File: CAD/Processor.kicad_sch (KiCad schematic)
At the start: 78 parts, among them M1 FID, M11 MOUNTING, M12 Logo_KICAD, M15 MOUNTING, M2 FID, M3 MOUNTING, M9 MOUNTING, U11 ATSAME70Q20B-AN, X1 ECS-120-10-33B-CKM-TR

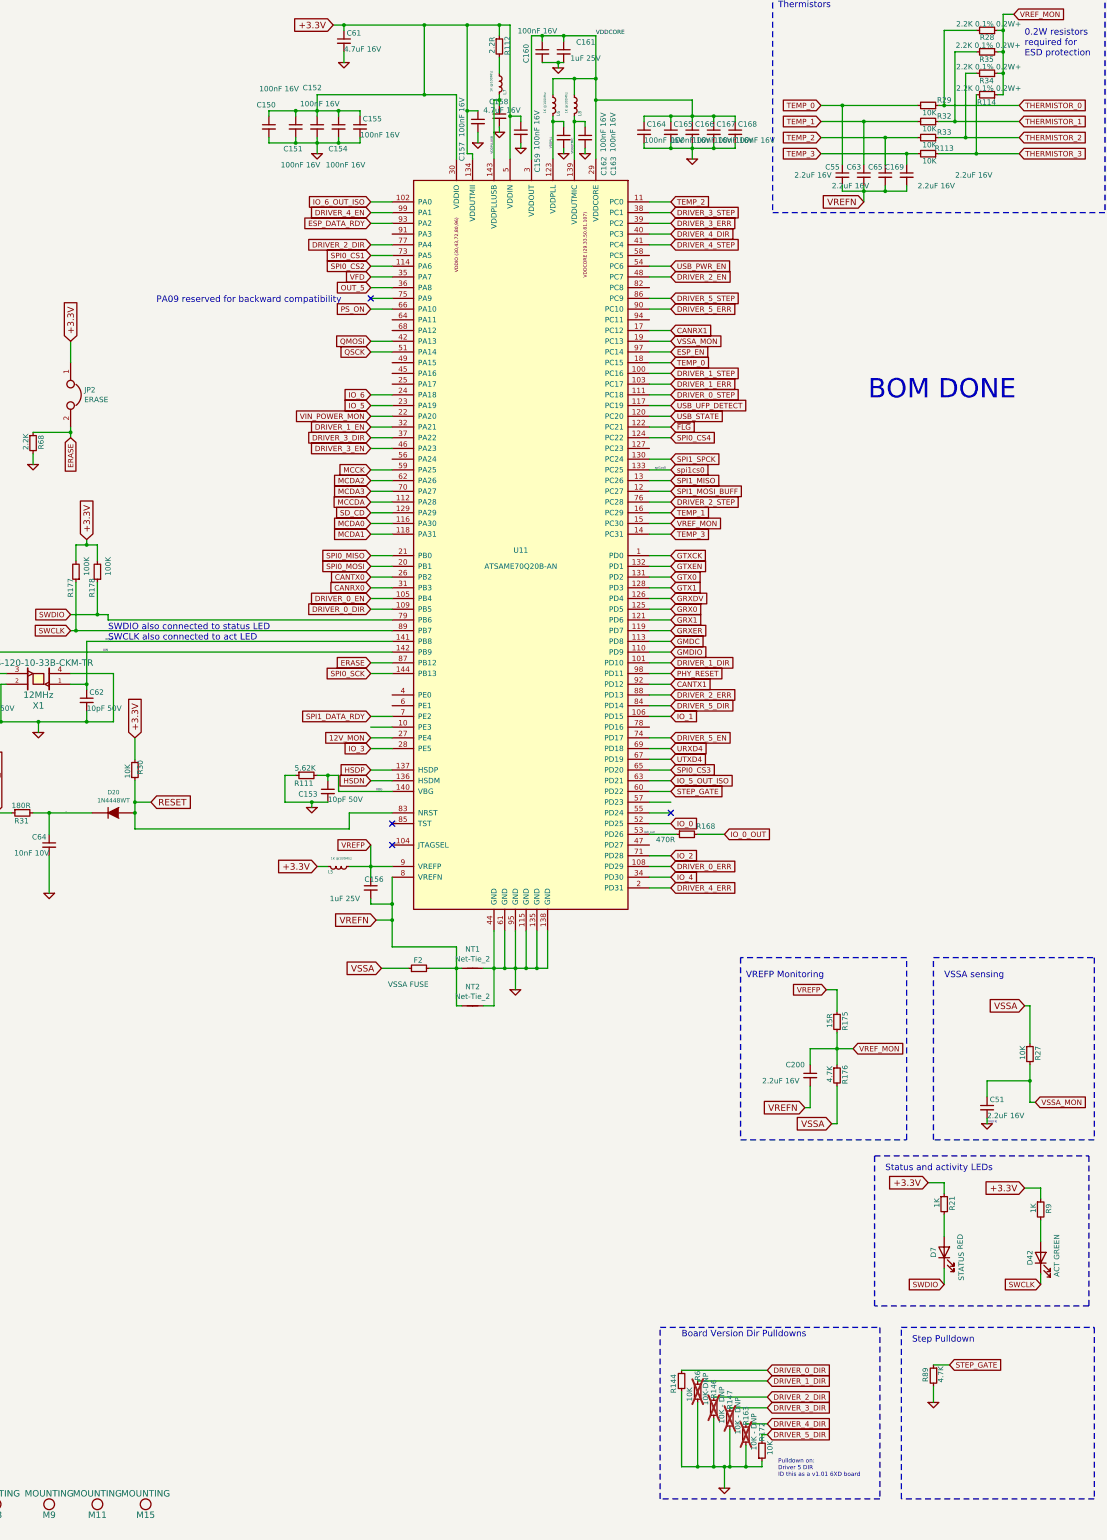
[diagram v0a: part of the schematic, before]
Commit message: WIP redoing board for new print
Removed version resistors.
Added pull-up on CMD.
Working on motors, not routed.
Added local library for custom parts.
Ran auto-cleanup of traces and vias (supervised).
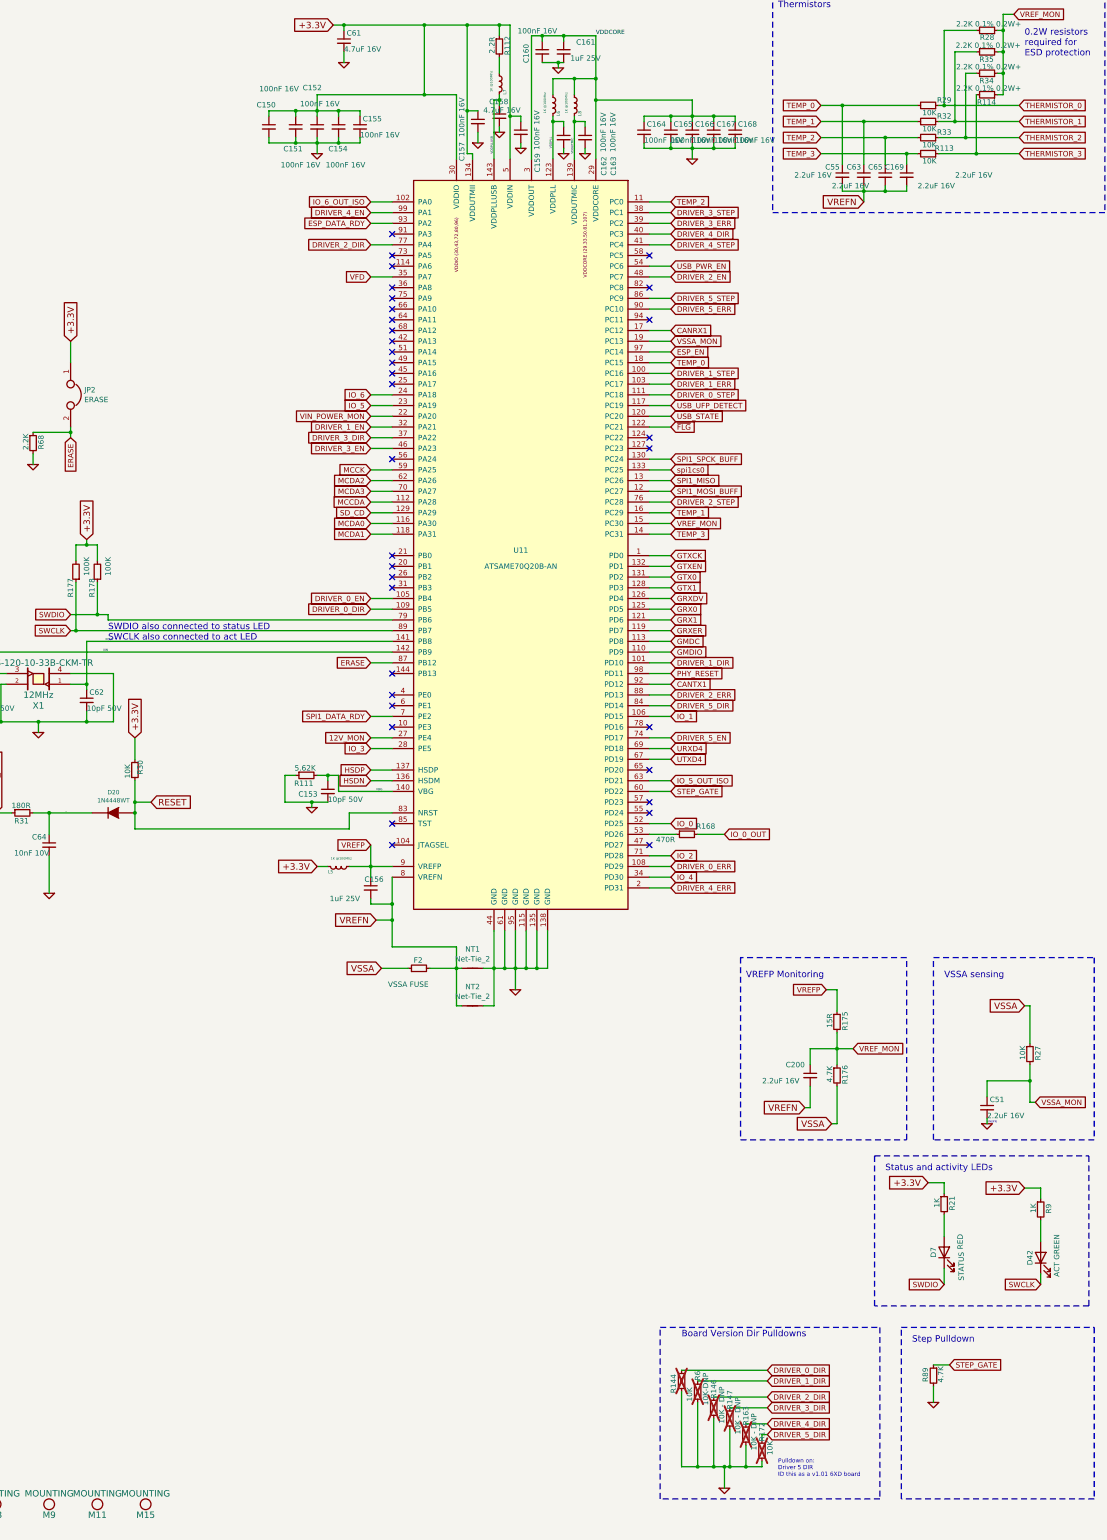
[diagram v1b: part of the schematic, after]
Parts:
- R144, R172: now not fitted; now left out of the parts list
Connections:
- net CANRX0: no longer names the net of U11.31 (PB3)
- net CANTX0: no longer names the net of U11.26 (PB2)
- net OUT_5: no longer names the net of U11.36 (PA8)
- net PS_ON: no longer names the net of U11.66 (PA10)
- net QMOSI: no longer names the net of U11.42 (PA13)
- net QSCK: no longer names the net of U11.51 (PA14)
- net SPI0_CS1: no longer names the net of U11.73 (PA5)
- net SPI0_CS2: no longer names the net of U11.114 (PA6)
- net SPI0_CS3: no longer names the net of U11.65 (PD20)
- net SPI0_CS4: no longer names the net of U11.124 (PC22)
- net SPI0_MISO: no longer names the net of U11.21 (PB0)
- net SPI0_MOSI: no longer names the net of U11.20 (PB1)
- net SPI0_SCK: no longer names the net of U11.144 (PB13)
- net SPI1_SPCK renamed SPI1_SPCK_BUFF
- net io0_out: no longer names the net of R168.1, U11.53 (PD26)
- no-connect marks 4 -> 34
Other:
- note removed: "BOM DONE"
- note removed: "PA09 reserved for backward compatibility"
- company: Duet3d -> 3DPotter
- title: Duet 3 Main Board 6XD -> Duet 3 Main Board 3DP

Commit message: update processor order info
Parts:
- U11: value ATSAME70Q20B-AN -> ATSAME70Q20B-ANT; LCSC C612779 -> C612769
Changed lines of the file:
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@@
 			)
 		)
-		(property "Value" "ATSAME70Q20B-AN"
+		(property "Value" "ATSAME70Q20B-ANT"
 			(at 144.78 149.86 0)
 			(effects
@@
 			)
 		)
-		(property "LCSC" "C612779"
+		(property "LCSC" "C612769"
 			(at 144.78 144.78 0)
 			(effects

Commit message: update led resistors
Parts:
- R21, R9: LCSC C144773 -> C144789
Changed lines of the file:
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@@
 			)
 		)
-		(property "LCSC" "C144773"
+		(property "LCSC" "C144789"
 			(at 245.11 300.99 90)
 			(effects
@@
 			)
 		)
-		(property "LCSC" "C144773"
+		(property "LCSC" "C144789"
 			(at 267.97 302.26 90)
 			(effects

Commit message: Change/Fix Ferrite Beads
L6-L8 Changed back to original values, no clue why I changed them in the first place
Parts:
- L6, L7, L8: LCSC C35061 -> C454079; Part Number GZ1608D102TF -> BK1608HS102-T
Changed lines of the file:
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@@
 			)
 		)
-		(property "Part Number" "GZ1608D102TF"
+		(property "Part Number" "BK1608HS102-T"
 			(at 152.4 40.64 0)
 			(effects
@@
 			)
 		)
-		(property "LCSC" "C35061"
+		(property "LCSC" "C454079"
 			(at 152.4 40.64 0)
 			(effects
@@
 			)
 		)
-		(property "Part Number" "GZ1608D102TF"
+		(property "Part Number" "BK1608HS102-T"
 			(at 139.7 35.56 0)
 			(effects
@@
 			)
 		)
-		(property "LCSC" "C35061"
+		(property "LCSC" "C454079"
 			(at 139.7 35.56 0)
 			(effects
@@
 			)
 		)
-		(property "Part Number" "GZ1608D102TF"
+		(property "Part Number" "BK1608HS102-T"
 			(at 157.48 40.64 0)
 			(effects
@@
 			)
 		)
-		(property "LCSC" "C35061"
+		(property "LCSC" "C454079"
 			(at 157.48 40.64 0)
 			(effects

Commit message: Replace Obsolete Parts
It appears that taiyo yuden is phasing out all BK1608 series ferrite beads, changing L5-L8 back to GZ1608D102TF for now.
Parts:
- L5, L6, L7, L8: LCSC C454079 -> C35061; Part Number BK1608HS102-T -> GZ1608D102TF
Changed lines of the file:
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@@
 			)
 		)
-		(property "Part Number" "BK1608HS102-T"
+		(property "Part Number" "GZ1608D102TF"
 			(at 152.4 40.64 0)
 			(effects
@@
 			)
 		)
-		(property "LCSC" "C454079"
+		(property "LCSC" "C35061"
 			(at 152.4 40.64 0)
 			(effects
@@
 			)
 		)
-		(property "Part Number" "BK1608HS102-T"
+		(property "Part Number" "GZ1608D102TF"
 			(at 139.7 35.56 0)
 			(effects
@@
 			)
 		)
-		(property "LCSC" "C454079"
+		(property "LCSC" "C35061"
 			(at 139.7 35.56 0)
 			(effects
@@
 			)
 		)
-		(property "Part Number" "BK1608HS102-T"
+		(property "Part Number" "GZ1608D102TF"
 			(at 157.48 40.64 0)
 			(effects
@@
 			)
 		)
-		(property "LCSC" "C454079"
+		(property "LCSC" "C35061"
 			(at 157.48 40.64 0)
 			(effects
@@
 			)
 		)
-		(property "Part Number" "BK1608HS102-T"
+		(property "Part Number" "GZ1608D102TF"
 			(at 101.6 220.98 0)
 			(effects
@@
 			)
 		)
-		(property "LCSC" "C454079"
+		(property "LCSC" "C35061"
 			(at 101.6 220.98 0)
 			(effects

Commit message: LM70860 Schematic: DONE
Schematic Finished, physical layout next
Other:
- note added: "Should this be pullup since the gates are active low?"
- note added: "Unused"
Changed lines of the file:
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@@
+		)
+	)
+	(text "Should this be pullup since\nthe gates are active low?"
+		(exclude_from_sim no)
+		(at 262.128 344.678 0)
+		(effects
+			(font
+				(size 1.524 1.524)
+			)
 		)
 	)
@@
 		)
 	)
+	(text "Unused\n"
+		(exclude_from_sim no)
+		(at 94.488 190.754 0)
+		(effects
+			(font
+				(size 1.524 1.524)
+			)
+		)
+	)
